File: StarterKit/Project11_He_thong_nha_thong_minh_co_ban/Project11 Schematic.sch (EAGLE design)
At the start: 13 parts, among them U1 ARDUINOR3-BPLACE

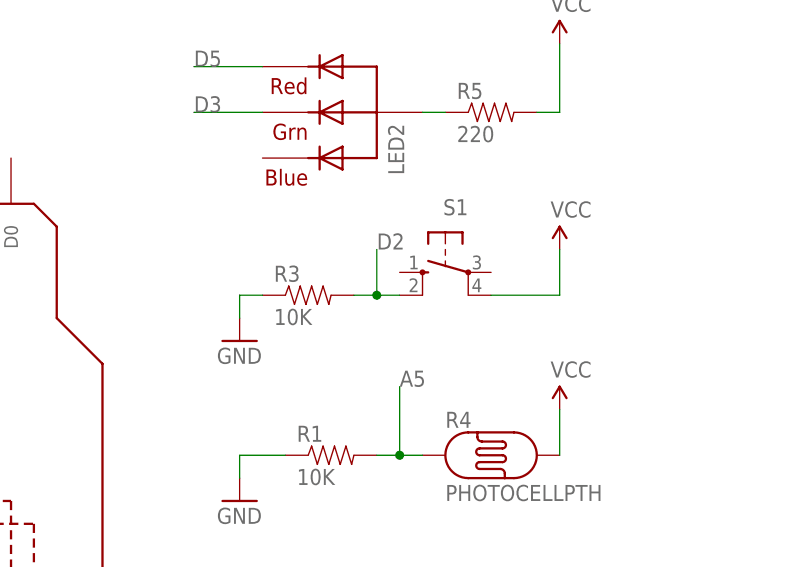
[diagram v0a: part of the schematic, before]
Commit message: Chuyen tu dien tro keo thap (pull-down) sang keo cao (pull-up) cho project 1a,1b,1c,7,11.
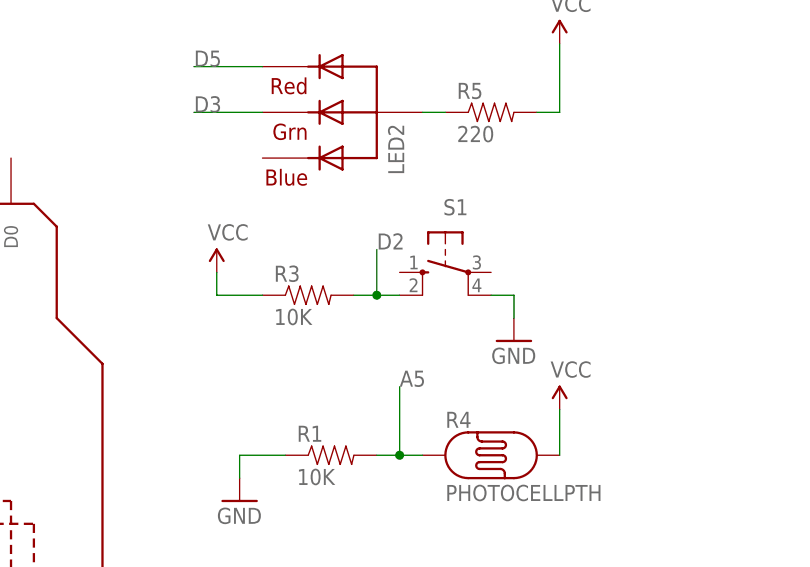
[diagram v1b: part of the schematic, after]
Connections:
- net GND: now also S1.P1; no longer R3.1
- net VCC: now also R3.1; no longer S1.P1
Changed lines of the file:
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@@
 <instance part="SUPPLY3" gate="G$1" x="160.02" y="121.92"/>
 <instance part="R3" gate="G$1" x="132.08" y="93.98"/>
-<instance part="SUPPLY4" gate="G$1" x="160.02" y="99.06"/>
+<instance part="SUPPLY4" gate="G$1" x="121.92" y="96.52"/>
 <instance part="GND4" gate="1" x="144.78" y="35.56"/>
-<instance part="GND5" gate="1" x="124.46" y="88.9"/>
+<instance part="GND5" gate="1" x="154.94" y="88.9"/>
 <instance part="LED2" gate="G$1" x="134.62" y="114.3" rot="R180"/>
 <instance part="R5" gate="G$1" x="152.4" y="114.3"/>
@@
 </segment>
 <segment>
-<pinref part="S1" gate="1" pin="P1"/>
-<pinref part="SUPPLY4" gate="G$1" pin="VCC"/>
-<wire x1="152.4" y1="93.98" x2="160.02" y2="93.98" width="0.1524" layer="91"/>
-<wire x1="160.02" y1="93.98" x2="160.02" y2="99.06" width="0.1524" layer="91"/>
-</segment>
-<segment>
 <pinref part="SUPPLY3" gate="G$1" pin="VCC"/>
 <wire x1="160.02" y1="121.92" x2="160.02" y2="114.3" width="0.1524" layer="91"/>
@@
 <wire x1="121.92" y1="35.56" x2="124.46" y2="35.56" width="0.1524" layer="91"/>
 </segment>
+<segment>
+<pinref part="SUPPLY4" gate="G$1" pin="VCC"/>
+<wire x1="121.92" y1="96.52" x2="121.92" y2="93.98" width="0.1524" layer="91"/>
+<pinref part="R3" gate="G$1" pin="1"/>
+<wire x1="121.92" y1="93.98" x2="127" y2="93.98" width="0.1524" layer="91"/>
+</segment>
 </net>
 <net name="GND" class="0">
@@
 </segment>
 <segment>
-<pinref part="R3" gate="G$1" pin="1"/>
-<pinref part="GND5" gate="1" pin="GND"/>
-<wire x1="127" y1="93.98" x2="124.46" y2="93.98" width="0.1524" layer="91"/>
-<wire x1="124.46" y1="93.98" x2="124.46" y2="91.44" width="0.1524" layer="91"/>
-</segment>
-<segment>
 <pinref part="U$1" gate="G$1" pin="GND"/>
 <pinref part="GND4" gate="1" pin="GND"/>
@@
 <wire x1="2.54" y1="91.44" x2="2.54" y2="88.9" width="0.1524" layer="91"/>
 </segment>
+<segment>
+<pinref part="GND5" gate="1" pin="GND"/>
+<wire x1="154.94" y1="91.44" x2="154.94" y2="93.98" width="0.1524" layer="91"/>
+<pinref part="S1" gate="1" pin="P1"/>
+<wire x1="154.94" y1="93.98" x2="152.4" y2="93.98" width="0.1524" layer="91"/>
+</segment>
 </net>
